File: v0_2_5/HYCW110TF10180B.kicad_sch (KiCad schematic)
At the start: 7 parts, among them J2 HYCW110-TF10-180B

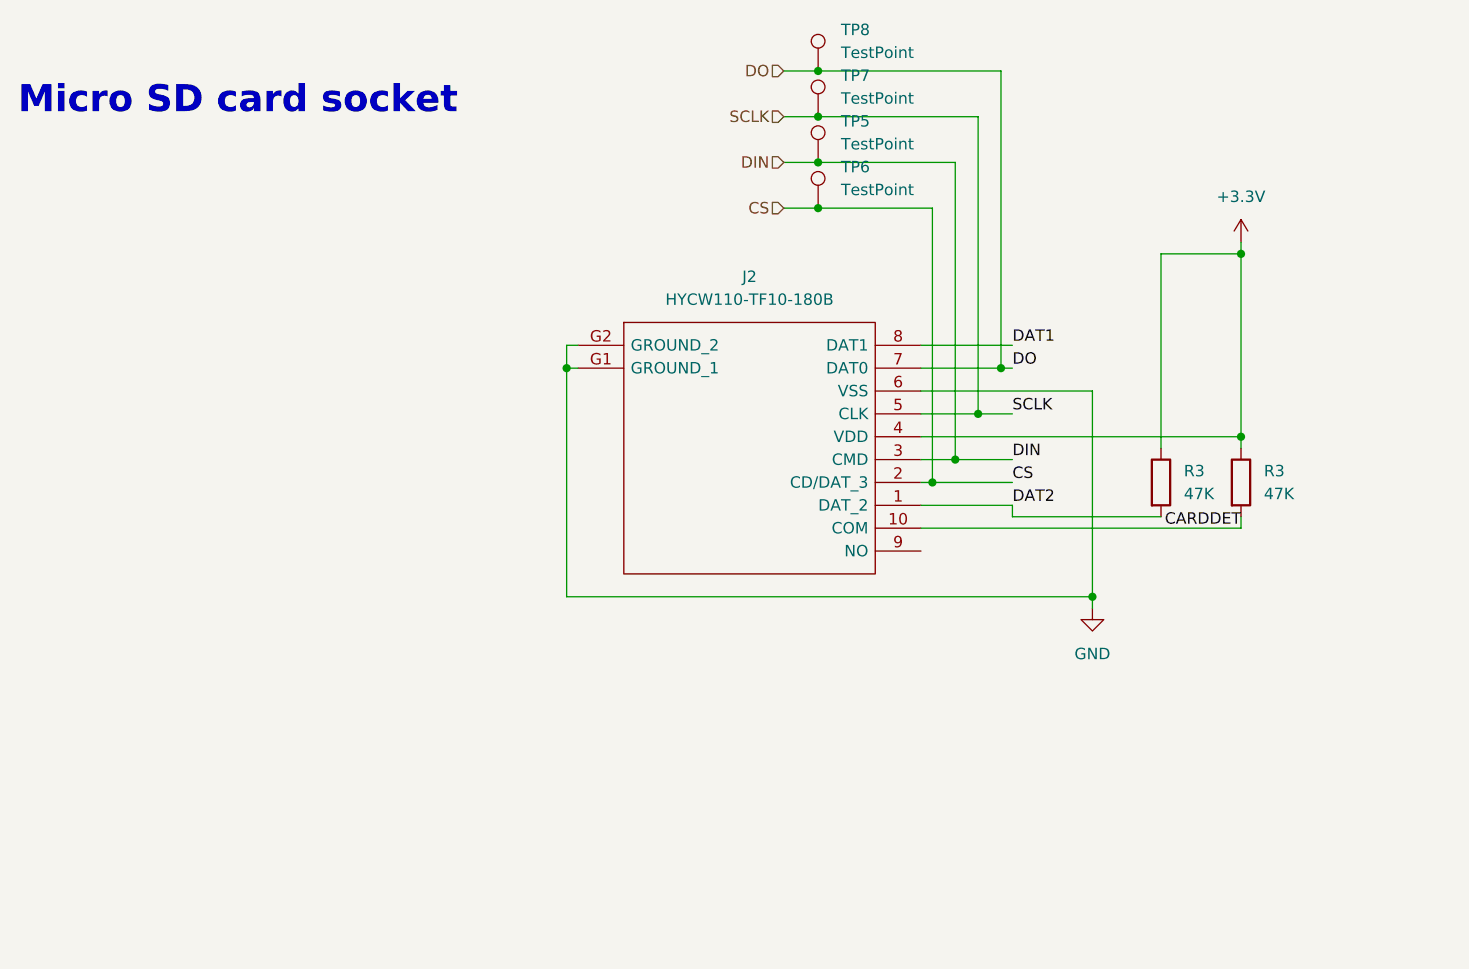
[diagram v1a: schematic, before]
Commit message: replace sdcard
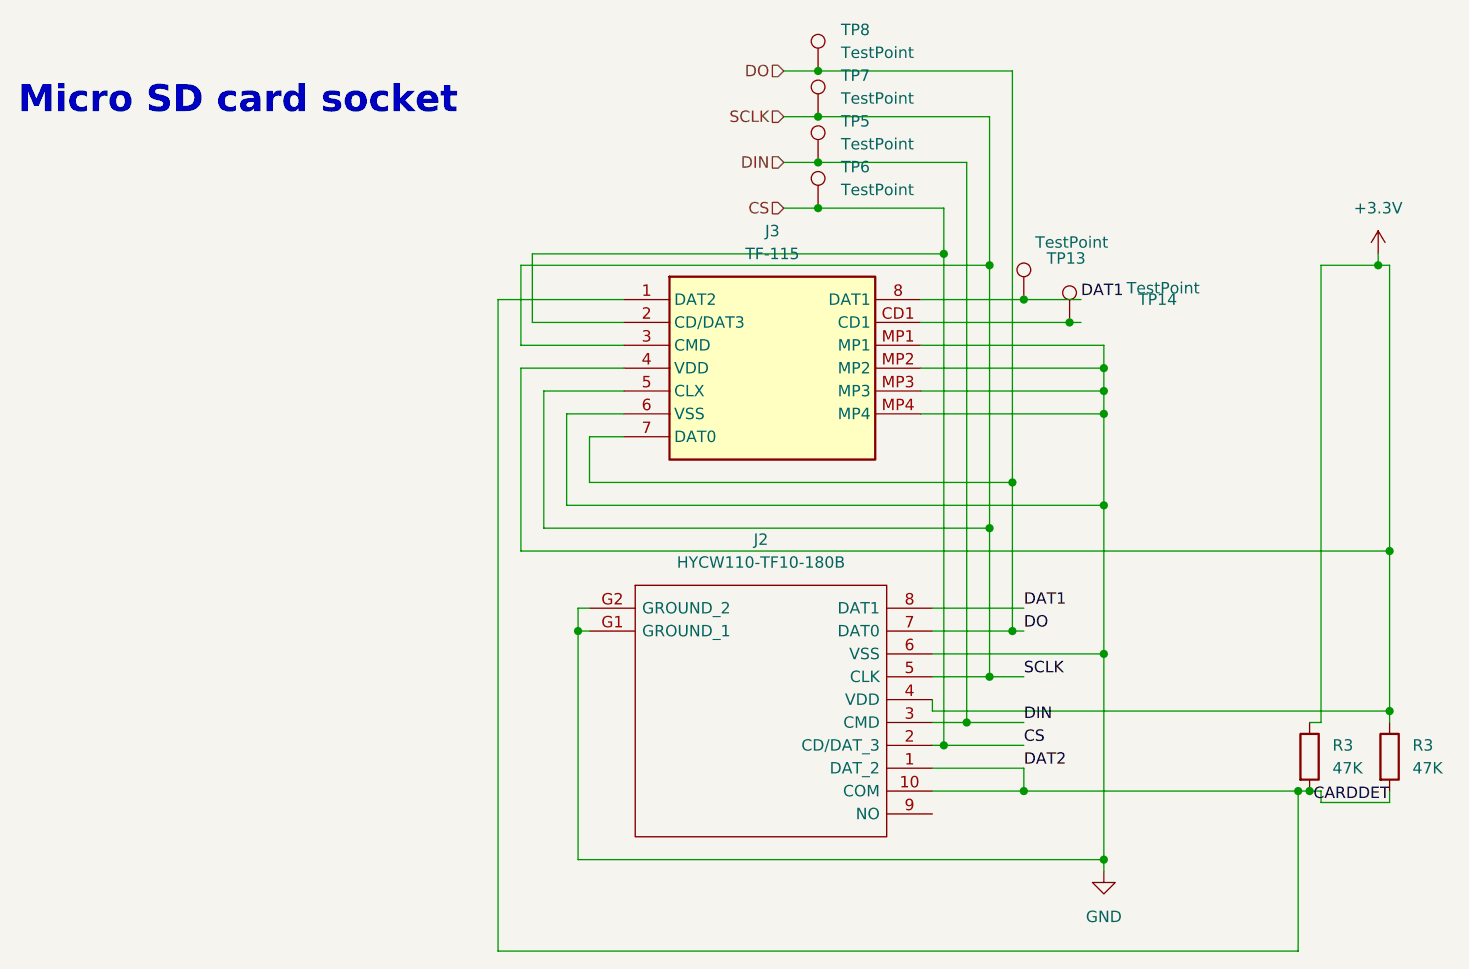
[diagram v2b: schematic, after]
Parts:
- added J3: TF-115, TF-115:TF115, symbol TF-115:TF-115
- added TP13, TP14: TestPoint, TestPoint:TestPoint_Pad_D1.0mm, symbol Connector:TestPoint
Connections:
- net DAT2 is gone; now on net CARDDET: J2.1 (DAT_2), R3.2
- net +3.3V: now also J3.4 (VDD)
- net CARDDET: now also J3.1 (DAT2)
- net CS: now also J3.2 (CD/DAT3)
- net DAT1: now also J3.8 (DAT1), TP13.1
- net DO: now also J3.7 (DAT0)
- net GND: now also J3.6 (VSS), J3.MP1, J3.MP2, J3.MP3, J3.MP4
- net SCLK: now also J3.3 (CMD), J3.5 (CLX)
- new net: J3.CD1, TP14.1
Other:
- moved on the sheet: J2, R3

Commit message: replace sdcard
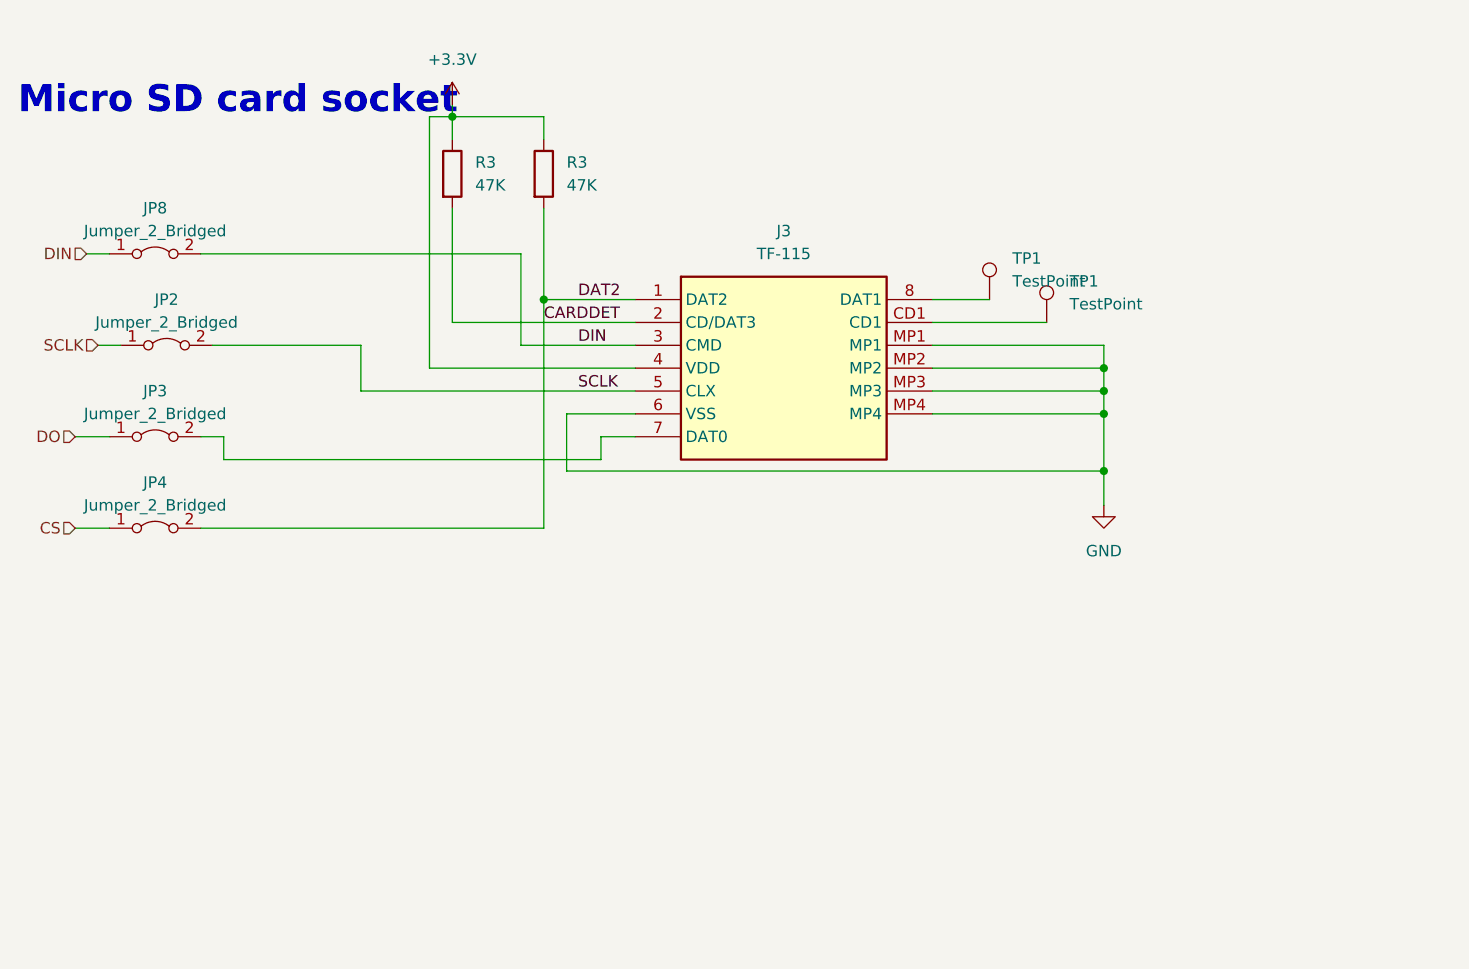
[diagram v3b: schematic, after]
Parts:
- removed J2: HYCW110-TF10-180B, HYCW110-TF10-180B:HYCW110TF10180B, symbol HYCW110-TF10-180B:HYCW110-TF10-180B
- removed TP13, TP14, TP5, TP6, TP7, TP8: TestPoint, TestPoint:TestPoint_Pad_D1.0mm, symbol Connector:TestPoint
- added JP2, JP3, JP4, JP8: Jumper_2_Bridged, Jumper:SolderJumper-2_P1.3mm_Bridged_RoundedPad1.0x1.5mm, symbol Jumper:Jumper_2_Bridged
- added TP1 (x2): TestPoint, TestPoint:TestPoint_Pad_D1.0mm, symbol Connector:TestPoint
- J3: LCSC Part # (none) -> C266620
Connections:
- net CARDDET: now also J3.2 (CD/DAT3), JP4.2 (B)
- net CS: now also JP4.1 (A); no longer J3.2 (CD/DAT3)
- net DIN: now also J3.3 (CMD), JP8.1 (A), JP8.2 (B)
- net DO: now also JP3.1 (A); no longer J3.7 (DAT0)
- net SCLK: now also JP2.1 (A), JP2.2 (B); no longer J3.3 (CMD)
- net at J3.CD1: now also TP1.1
- net DAT1: no longer names the net of J3.8 (DAT1)
- net DAT1: now also TP1.1
- new net: J3.7 (DAT0), JP3.2 (B)
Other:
- moved on the sheet: J3, R3
